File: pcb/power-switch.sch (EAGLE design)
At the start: 22 parts, among them CON1 KF301-3P, CON2 KF301-3P, K1 SMIH-12VDC-S-L-C, K2 SMIH-12VDC-S-L-C, U1 MCP1631X, U6 EFM32PG1B200_Q32, U7 RFM69HW

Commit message: PCB Work
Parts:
- added C4: 1uF, Capacitor:CAPACITOR-1206
- added C5: 100nF, Capacitor:CAPACITOR-0603
- added D1, D2: B0530W, Generic Diode:B0530W
- added D3: SMAJ12A, TVS:SMAJ12A
- added F1: 500mA Hold, PTC Fuses:PTC1812
- added Q1, Q2: AO3400, Alpha Omega:AO3400
- added R1, R3: 22 Ohms, Resistor:RESISTOR-0603
- added R2, R5: 100K Ohms, Resistor:RESISTOR-0603
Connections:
- new net K1_EN: R1.2
- new net K2_EN: R3.2
- new net N$2: Q1.G, R1.1, R2.1
- new net N$3: D1.A, K1.COIL2, Q1.D
- new net N$4: Q2.G, R3.1, R5.1
- new net N$5: D2.A, K2.COIL2, Q2.D
- new net N$7: ACDC1.+VO, F1.2
- net 12V0: now also C4.C1, C5.C1, D1.C, D2.C, D3.C, F1.1, K1.COIL1, K2.COIL1; no longer ACDC1.+VO
- net GND: now also ACDC1.-VO, C4.C2, C5.C2, D3.A, Q1.S, Q2.S, R2.2, R5.2
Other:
- moved on the sheet: CON1-1, CON1-2, CON1-3, CON2-1, CON2-2, CON2-3, K1, K2, MOV1, U1

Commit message: PCB Work
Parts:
- removed C4: 1uF, Capacitor:CAPACITOR-1206
- added C10, C11, C12, C13, C20, C6: 100nF, Capacitor:CAPACITOR-0603
- added C7: 1uF, Capacitor:CAPACITOR-0603
- added C8, C9: 100uF, Capacitor:CAPACITOR-1206
- added CON3: 4P-SH-TOP, JST:4P-SH-TOP
- added L2: 15uH, Inductor:INDUCTOR-2.5X2X1.2MM
- added R10, R15, R6, R8, R9: 10K Ohms, Resistor:RESISTOR-0603
- added R16: 100K Ohms, Resistor:RESISTOR-0603
- added R7: 31.6K Ohms, Resistor:RESISTOR-0603
- added U2: MCP9802, Microchip:MCP9802
- added U8: SST26VF016B, Microchip:SST26VF016B
- added X1: 40MHz, Crystal:CRYSTAL_4P
- R14, R4: value 10K Ohms -> 100K Ohms
- TC1: value TC2050-IDC -> TC2050-IDC-NL; device TagConnect:TC2050-IDC -> TagConnect:TC2050-IDC-NL
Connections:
- new net !FLASH_CS: R16.1, U8.!CS!
- new net BTN1: C13.C1, CON3-2.S, R10.1
- new net BTN2: C12.C1, CON3-3.S, R9.1
- new net I2C0_SCL: R15.1, U2.SCL
- new net I2C0_SDA: R8.1, U2.SDA
- new net N$10: R6.2, R7.1, U1.FB
- new net N$16: U6.HFXTAL_N, X1.1
- new net N$17: U6.HFXTAL_P, X1.2
- new net N$6: C6.C2, L2.1, U1.SW
- new net N$8: C6.C1, U1.BOOST
- new net N$9: C7.C1, U1.VCC
- new net TEMP_ALERT: U2.ALERT
- net 12V0: now also C8.C1, U1.EN, U1.VIN; no longer C4.C1
- net 3V3: now also C10.C1, C11.C1, C20.C1, C9.C1, L2.2, R10.2, R15.2, R16.2, R7.2, R8.2, R9.2, U2.VDD, U8.!HOLD!/IO3, U8.!WP!/IO2, U8.VCC
- net GND: now also C10.C2, C11.C2, C12.C2, C13.C2, C20.C2, C7.C2, C8.C2, C9.C2, CON3-1.S, CON3-4.S, R6.1, U1.AGND, U1.PGND, U2.GND, U8.GND, X1.GND@0, X1.GND@1; no longer C4.C2
- net US0_CLK: now also U8.SCK
- net US0_MISO: now also U8.MISO/IO1
- net US0_MOSI: now also U8.MOSI/IO0

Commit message: Finished PCB
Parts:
- added D4, D5: LED1206, LED:LED1206
- added LOGO1: HV_WARNING, Silkscreen:HV_WARNING
- added R11, R12: 2.2K Ohms, Resistor:RESISTOR-0603
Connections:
- removed net TEMP_ALERT: U2.ALERT
- new net N$11: D4.A, R11.1
- new net N$12: D5.A, R12.1
- net !FLASH_CS: now also U6.PC11
- net !RFM_CS: now also U6.PB12; no longer U6.PD12
- net 12V0: now also R11.2, R12.2
- net BTN1: now also U6.PD9
- net BTN2: now also U6.PD10
- net I2C0_SCL: now also U6.PD13
- net I2C0_SDA: now also U6.PD12
- net K1_EN: now also U6.PA0
- net K2_EN: now also U6.PA1
- net N$3: now also D4.C
- net N$5: now also D5.C
- net RFM_RST: now also U6.PB11; no longer U6.PD11
- net US0_CLK: now also U6.PB13; no longer U6.PD13
- net US0_MISO: now also U6.PB15; no longer U6.PD15
- net US0_MOSI: now also U6.PB14; no longer U6.PD14

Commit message: Update libs
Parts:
- U1: value MCP1631X -> MCP16311; device Microchip:MCP1631X -> Microchip:MCP16311
- U2: value MCP9802 -> MCP9802-A0; device Microchip:MCP9802 -> Microchip:MCP9802-A0
- U6: value EFM32PG1B200_Q32 -> EFM32PG1B200F256GM32; device EFM32:EFM32PG1B200_Q32 -> EFM32:EFM32PG1B200F256GM32
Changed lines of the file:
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@@
 <part name="2V1" library="Supply Symbol" deviceset="3V3" device=""/>
 <part name="GND11" library="Supply Symbol" deviceset="GND" device=""/>
-<part name="U6" library="EFM32" deviceset="EFM32PG1B200_Q32" device=""/>
+<part name="U6" library="EFM32" deviceset="EFM32PG1B200F*M32" device="" technology="256G"/>
 <part name="FRAME2" library="Frame" deviceset="A3-LANDSCAPE" device=""/>
 <part name="L1" library="Inductor" deviceset="INDUCTOR" device="-0603" value="4.7uH">
@@
 <part name="GND5" library="Supply Symbol" deviceset="GND" device=""/>
 <part name="2V6" library="Supply Symbol" deviceset="3V3" device=""/>
-<part name="U1" library="Microchip" deviceset="MCP1631X" device=""/>
+<part name="U1" library="Microchip" deviceset="MCP1631*" device="" technology="1"/>
 <part name="ACDC1" library="ACDC Converter" deviceset="HLK-PM" device="12"/>
 <part name="CON1" library="Generic Connector" deviceset="KF301-3P" device=""/>
@@
 <part name="2V14" library="Supply Symbol" deviceset="3V3" device=""/>
 <part name="2V15" library="Supply Symbol" deviceset="3V3" device=""/>
-<part name="U2" library="Microchip" deviceset="MCP9802" device=""/>
+<part name="U2" library="Microchip" deviceset="MCP9802-A*" device="" technology="0"/>
 <part name="CON3" library="JST" deviceset="4P" device="-SH-TOP"/>
 <part name="R9" library="Resistor" deviceset="RESISTOR" device="-0603" value="10K Ohms"/>

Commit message: Fix crystal package
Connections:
- net AC_L: now also K1.COM, K2.COM; no longer K1.COM1, K2.COM1
- net AC_L_K1: now also K1.NO; no longer K1.NO1
- net AC_L_K2: now also K2.NO; no longer K2.NO1
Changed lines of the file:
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@@
 <?xml version="1.0" encoding="utf-8"?>
 <!DOCTYPE eagle SYSTEM "eagle.dtd">
-<eagle version="9.3.2">
+<eagle version="9.4.2">
 <drawing>
 <settings>
@@
 <part name="2V3" library="Supply Symbol" deviceset="3V3" device=""/>
 <part name="GND3" library="Supply Symbol" deviceset="GND" device=""/>
-<part name="U7" library="HopeRF" deviceset="RFM69H" device="W" value="RFM69HW"/>
+<part name="U7" library="HopeRF" deviceset="RFM69*" device="W" technology="H" value="RFM69HW"/>
 <part name="GND10" library="Supply Symbol" deviceset="GND" device=""/>
 <part name="C16" library="Capacitor" deviceset="CAPACITOR" device="-0603" value="100nF"/>
@@
 <wire x1="345.44" y1="116.84" x2="353.06" y2="116.84" width="0.1524" layer="91"/>
 <label x="353.06" y="116.84" size="1.778" layer="95" xref="yes"/>
-<pinref part="K2" gate="G$1" pin="NO1"/>
+<pinref part="K2" gate="G$1" pin="NO"/>
 </segment>
 </net>
@@
 <wire x1="342.9" y1="218.44" x2="350.52" y2="218.44" width="0.1524" layer="91"/>
 <label x="350.52" y="218.44" size="1.778" layer="95" xref="yes"/>
-<pinref part="K1" gate="G$1" pin="NO1"/>
+<pinref part="K1" gate="G$1" pin="NO"/>
 </segment>
 </net>
@@
 <wire x1="342.9" y1="226.06" x2="350.52" y2="226.06" width="0.1524" layer="91"/>
 <label x="350.52" y="226.06" size="1.778" layer="95" xref="yes"/>
-<pinref part="K1" gate="G$1" pin="COM1"/>
+<pinref part="K1" gate="G$1" pin="COM"/>
 </segment>
 <segment>
 <wire x1="345.44" y1="124.46" x2="353.06" y2="124.46" width="0.1524" layer="91"/>
 <label x="353.06" y="124.46" size="1.778" layer="95" xref="yes"/>
-<pinref part="K2" gate="G$1" pin="COM1"/>
-</segment>
-</net>
+<pinref part="K2" gate="G$1" pin="COM"/>
+</segment>
+</net>

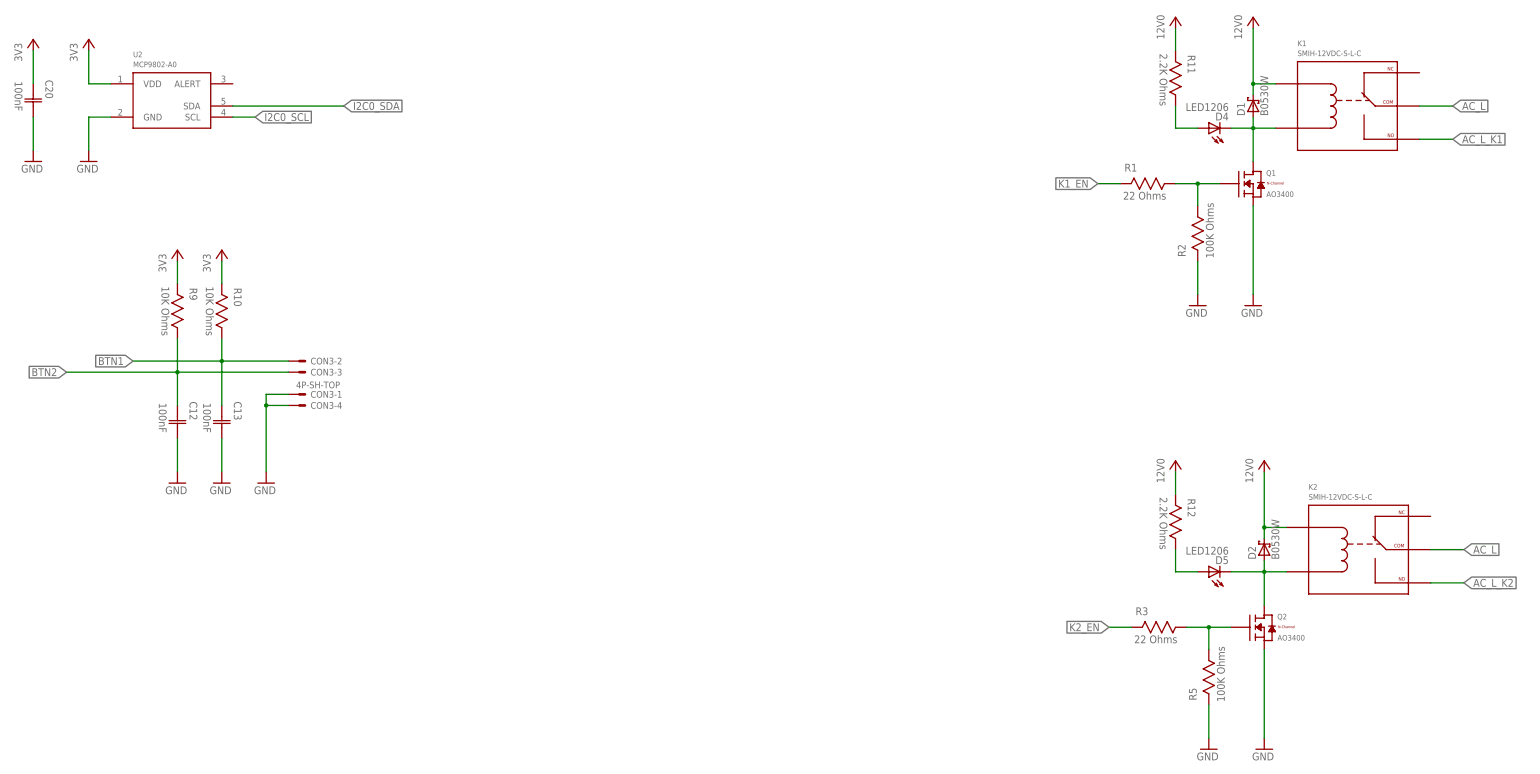
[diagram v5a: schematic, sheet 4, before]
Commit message: Sync library updates Add schematic PDF
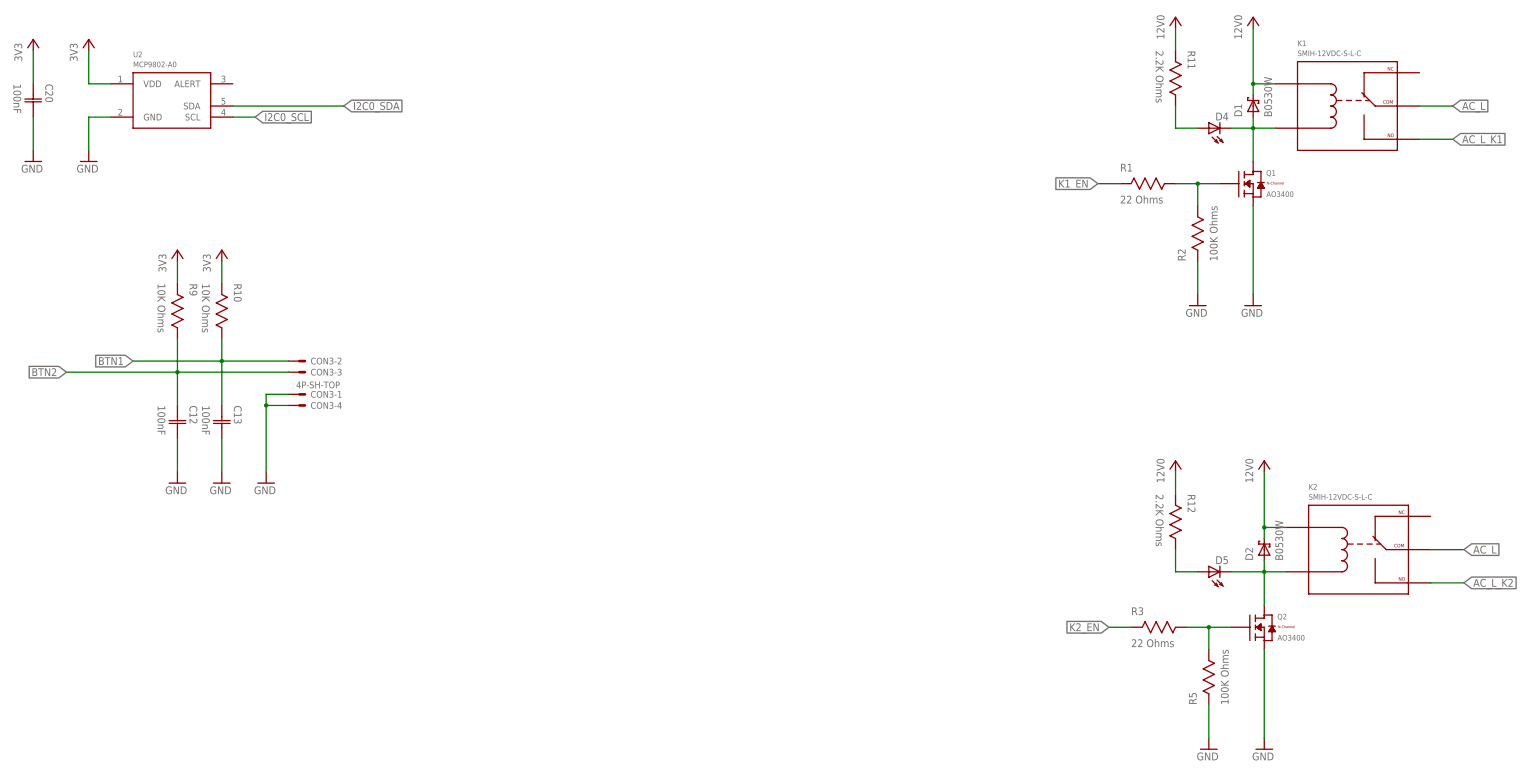
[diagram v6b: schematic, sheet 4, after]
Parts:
- F1: HOLD (none) -> 500mA
